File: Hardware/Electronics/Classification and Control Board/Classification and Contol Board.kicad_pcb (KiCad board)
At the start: 4 copper layers, 53.9 x 62.3 mm, 93 parts, among them J1 SWD Header, J10 USB_B_Mini, J2 Barrel_Jack, J3 Thumb, J4 Index, J5 Middle, J6 Ring, J7 Pinky, J8 Wrist, J9 HC05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

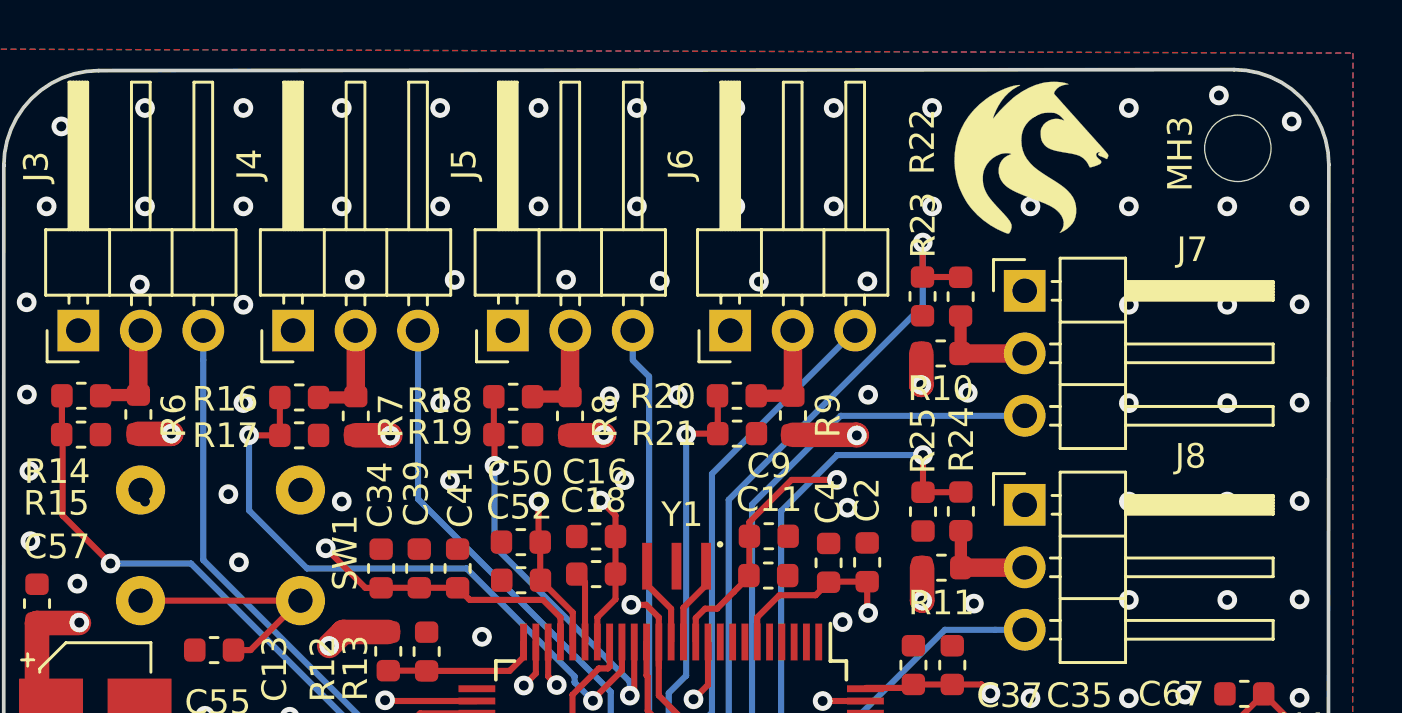
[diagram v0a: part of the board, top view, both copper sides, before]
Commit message: Ran the Gerbers, made fab layer look fab
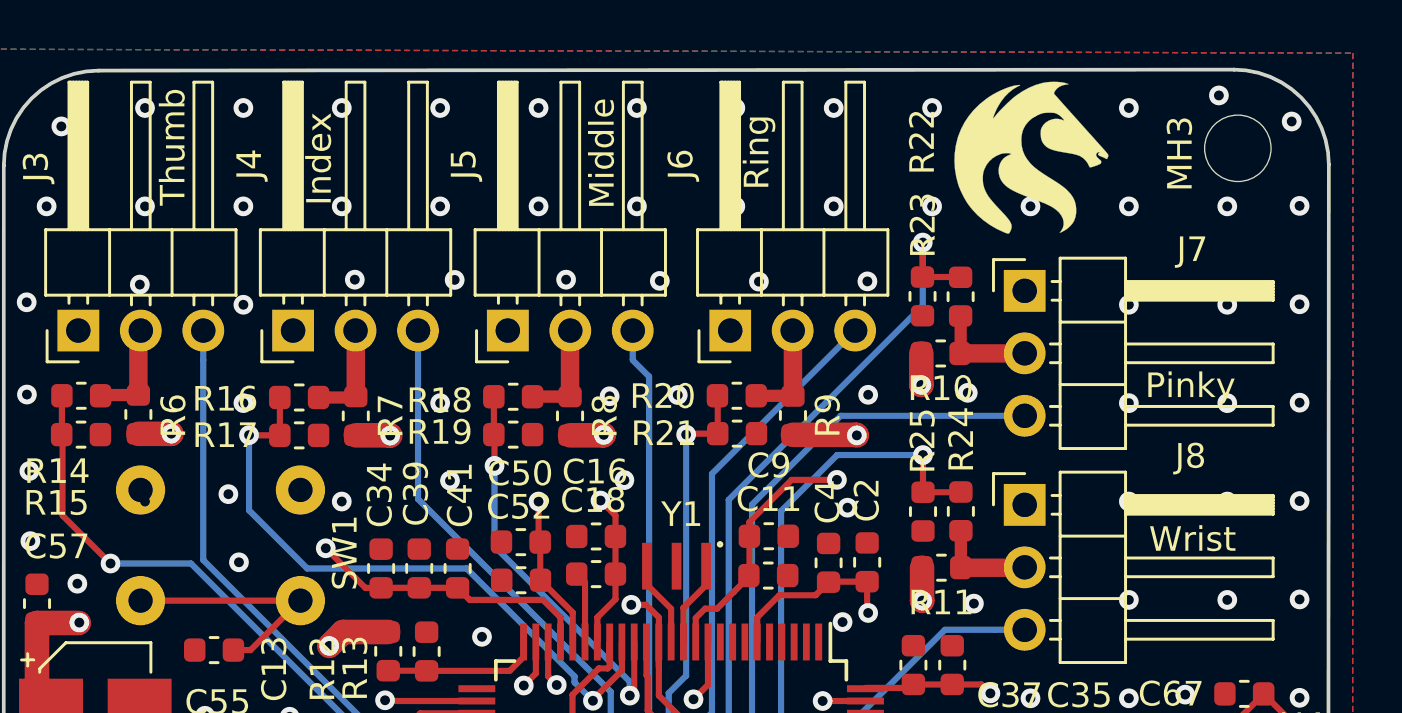
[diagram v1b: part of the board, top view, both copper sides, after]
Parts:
- MH1: value MountingHole -> (none)

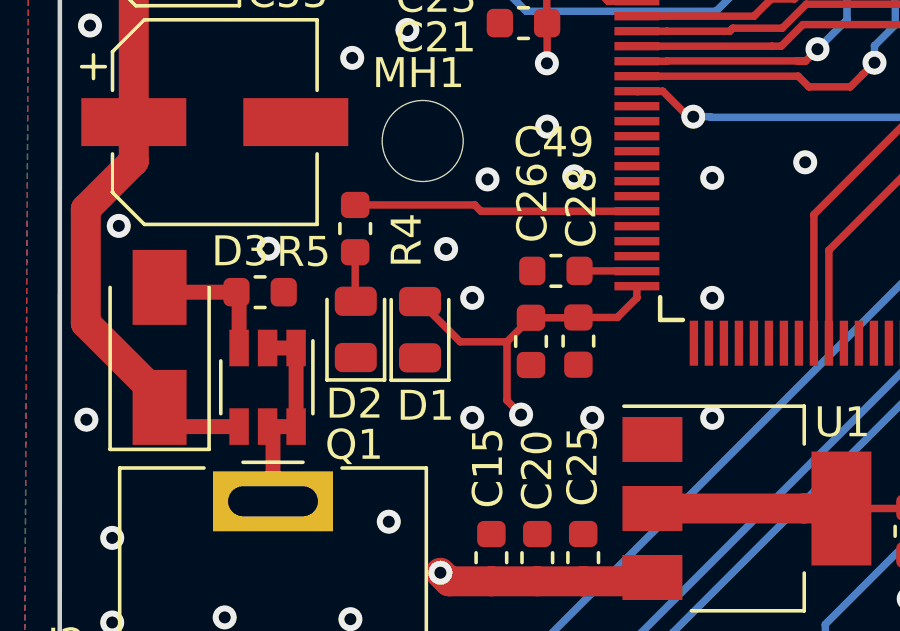
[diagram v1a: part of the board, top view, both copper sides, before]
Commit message: Changed blue LED to green and added current limiting resistor
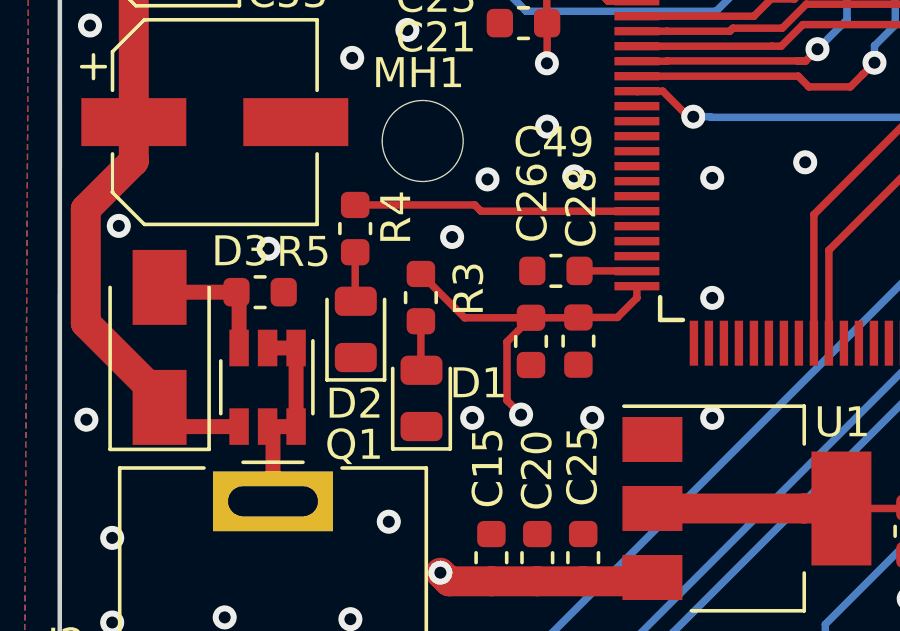
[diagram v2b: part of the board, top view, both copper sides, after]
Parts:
- added R3: 6R, Resistor_SMD:R_0603_1608Metric, F.Cu at (126.5, 98.8)
- D1: value LTST-C171TBKT -> LTST-C171TGKT
- MH1: value (none) -> MountingHole
- moved D1 2.29 mm to (126.5, 102.2)
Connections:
- D1 pad 2: /STM32F407VGTx/3V3 -> Net-(D1-Pad2)
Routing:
- net Net-(D1-Pad2): track 0.00 -> 1.64 mm
- net /STM32F407VGTx/3V3: track 89.5 -> 90.3 mm
- net /GND: vias 176 -> 175
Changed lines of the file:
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@@
     (thickness 1.6)
     (drawings 15)
-    (tracks 722)
+    (tracks 723)
     (zones 0)
-    (modules 93)
-    (nets 122)
+    (modules 94)
+    (nets 123)
   )
   (page A4)
@@
     (34 B.Paste user)
     (35 F.Paste user)
-    (36 B.SilkS user hide)
+    (36 B.SilkS user)
     (37 F.SilkS user)
     (38 B.Mask user)
@@
   (net 120 /Communications/BT_TX)
   (net 121 /Communications/BT_RX)
+  (net 122 "Net-(D1-Pad2)")
   (net_class Default "This is the default net class."
     (clearance 0.15)
@@
     (add_net "Net-(C51-Pad1)")
     (add_net "Net-(C61-Pad1)")
+    (add_net "Net-(D1-Pad2)")
     (add_net "Net-(D2-Pad2)")
     (add_net "Net-(D6-Pad2)")
@@
     (add_net /V+)
   )
+  (module Resistor_SMD:R_0603_1608Metric (layer F.Cu)
+    (at 126.47 98.82 90)
+    (descr "Resistor SMD 0603 (1608 Metric), square (rectangular) end terminal, IPC_7351 nominal, (Body size source: http://www.tortai-tech.com/upload/download/2011102023233369053.pdf), generated with kicad-footprint-generator")
+    (tags resistor)
+    (attr smd)
+    (fp_text reference R3 (at 0.3 1.6 90) (layer F.SilkS)
+      (effects (font (size 1 1) (thickness 0.15)))
+    )
+    (fp_text value 6R (at 0 1.43 90) (layer F.Fab)
+      (effects (font (size 1 1) (thickness 0.15)))
+    )
+    (fp_line (start -0.8 0.4) (end -0.8 -0.4) (layer F.Fab) (width 0.1))
+    (fp_line (start -0.8 -0.4) (end 0.8 -0.4) (layer F.Fab) (width 0.1))
+    (fp_line (start 0.8 -0.4) (end 0.8 0.4) (layer F.Fab) (width 0.1))
+    (fp_line (start 0.8 0.4) (end -0.8 0.4) (layer F.Fab) (width 0.1))
+    (fp_line (start -0.162779 -0.51) (end 0.162779 -0.51) (layer F.SilkS) (width 0.12))
+    (fp_line (start -0.162779 0.51) (end 0.162779 0.51) (layer F.SilkS) (width 0.12))
+    (fp_line (start -1.48 0.73) (end -1.48 -0.73) (layer F.CrtYd) (width 0.05))
+    (fp_line (start -1.48 -0.73) (end 1.48 -0.73) (layer F.CrtYd) (width 0.05))
+    (fp_line (start 1.48 -0.73) (end 1.48 0.73) (layer F.CrtYd) (width 0.05))
+    (fp_line (start 1.48 0.73) (end -1.48 0.73) (layer F.CrtYd) (width 0.05))
+    (fp_text user %R (at 0 0 90) (layer F.Fab)
+      (effects (font (size 0.4 0.4) (thickness 0.06)))
+    )
+    (pad 1 smd roundrect (at -0.7875 0 90) (size 0.875 0.95) (layers F.Cu F.Paste F.Mask) (roundrect_rratio 0.25)
+      (net 122 "Net-(D1-Pad2)"))
+    (pad 2 smd roundrect (at 0.7875 0 90) (size 0.875 0.95) (layers F.Cu F.Paste F.Mask) (roundrect_rratio 0.25)
+      (net 4 /STM32F407VGTx/3V3))
+    (model ${KISYS3DMOD}/Resistor_SMD.3dshapes/R_0603_1608Metric.wrl
+      (at (xyz 0 0 0))
+      (scale (xyz 1 1 1))
+      (rotate (xyz 0 0 0))
+    )
+  )
   (module Switches:1825910-6 (layer F.Cu)
     (at 120 78.36)
@@
   )
   (module LED_SMD:LED_0805_2012Metric (layer F.Cu)
-    (at 126.44 99.89 90)
+    (at 126.49 102.18 90)
     (descr "LED SMD 0805 (2012 Metric), square (rectangular) end terminal, IPC_7351 nominal, (Body size source: https://docs.google.com/spreadsheets/d/1BsfQQcO9C6DZCsRaXUlFlo91Tg2WpOkGARC1WS5S8t0/edit?usp=sharing), generated with kicad-footprint-generator")
     (tags diode)
     (attr smd)
-    (fp_text reference D1 (at -2.54 0.19 180) (layer F.SilkS)
+    (fp_text reference D1 (at 0.5 1.9 180) (layer F.SilkS)
       (effects (font (size 1 1) (thickness 0.15)))
     )
-    (fp_text value LTST-C171TBKT (at -32.12 -0.98 90) (layer F.Fab)
+    (fp_text value LTST-C171TGKT (at -32.12 -0.98 90) (layer F.Fab)
       (effects (font (size 1 1) (thickness 0.15)))
     )
@@
       (net 1 /GND))
     (pad 2 smd roundrect (at 0.9375 0 90) (size 0.975 1.4) (layers F.Cu F.Paste F.Mask) (roundrect_rratio 0.25)
-      (net 4 /STM32F407VGTx/3V3))
+      (net 122 "Net-(D1-Pad2)"))
     (model ${KISYS3DMOD}/LED_SMD.3dshapes/LED_0805_2012Metric.wrl
       (at (xyz 0 0 0))
@@
       (effects (font (size 1 1) (thickness 0.15)))
     )
-    (fp_text value " " (at -21.29 -1.82) (layer F.Fab)
+    (fp_text value MountingHole (at -21.29 -1.82) (layer F.Fab)
       (effects (font (size 1 1) (thickness 0.15)))
     )
@@
     (tags resistor)
     (attr smd)
-    (fp_text reference R4 (at 0.39 -1.72 270) (layer F.SilkS)
+    (fp_text reference R4 (at -0.37 -1.37 270) (layer F.SilkS)
       (effects (font (size 1 1) (thickness 0.15)))
     )
@@
   (via (at 130.68 93.12) (size 0.8) (drill 0.4) (layers F.Cu B.Cu) (net 1))
   (via (at 128.69 94.88) (size 0.8) (drill 0.4) (layers F.Cu B.Cu) (net 1))
-  (via (at 128.18 98.83) (size 0.8) (drill 0.4) (layers F.Cu B.Cu) (net 1))
   (via (at 128.18 102.83) (size 0.8) (drill 0.4) (layers F.Cu B.Cu) (net 1))
   (via (at 128.18 110.83) (size 0.8) (drill 0.4) (layers F.Cu B.Cu) (net 1))
@@
   (via (at 124 81.3) (size 0.8) (drill 0.4) (layers F.Cu B.Cu) (net 1))
   (via (at 124.18 90.83) (size 0.8) (drill 0.4) (layers F.Cu B.Cu) (net 1))
-  (via (at 127.31 97.2) (size 0.8) (drill 0.4) (layers F.Cu B.Cu) (net 1))
+  (via (at 127.51 96.8) (size 0.8) (drill 0.4) (layers F.Cu B.Cu) (net 1))
   (via (at 125.4 106.29) (size 0.8) (drill 0.4) (layers F.Cu B.Cu) (net 1))
   (via (at 124.12 109.54) (size 0.8) (drill 0.4) (layers F.Cu B.Cu) (net 1))
@@
   (segment (start 136.18 80.4125) (end 136.2475 80.48) (width 0.25) (layer F.Cu) (net 4))
   (segment (start 136.18 78.83) (end 136.18 80.4125) (width 0.25) (layer F.Cu) (net 4))
-  (segment (start 127.78001 100.29251) (end 126.44 98.9525) (width 0.25) (layer F.Cu) (net 4))
-  (segment (start 129.33999 100.29251) (end 127.78001 100.29251) (width 0.25) (layer F.Cu) (net 4))
   (segment (start 131.3675 87.44) (end 130.6675 88.14) (width 0.25) (layer F.Cu) (net 4))
   (segment (start 133.67 87.44) (end 131.3675 87.44) (width 0.25) (layer F.Cu) (net 4))
@@
   (segment (start 149.90001 104.64999) (end 149.90001 103.33251) (width 0.25) (layer F.Cu) (net 4))
   (segment (start 149.14 105.41) (end 149.90001 104.64999) (width 0.25) (layer F.Cu) (net 4))
+  (segment (start 127.93 99.4925) (end 126.47 98.0325) (width 0.25) (layer F.Cu) (net 4))
+  (segment (start 130.14 99.4925) (end 127.93 99.4925) (width 0.25) (layer F.Cu) (net 4))
   (segment (start 152.32 88.5325) (end 152.5225 88.33) (width 0.25) (layer F.Cu) (net 5))
   (segment (start 150.47 89.44) (end 149.47 89.44) (width 0.25) (layer F.Cu) (net 5))
@@
   (segment (start 150.995001 107.505001) (end 151.504005 107.505001) (width 0.25) (layer B.Cu) (net 121))
   (segment (start 150.59 107.1) (end 150.995001 107.505001) (width 0.25) (layer B.Cu) (net 121))
+  (segment (start 126.47 101.2225) (end 126.49 101.2425) (width 0.25) (layer F.Cu) (net 122))
+  (segment (start 126.47 99.6075) (end 126.47 101.2225) (width 0.25) (layer F.Cu) (net 122))
   (zone (net 1) (net_name /GND) (layer F.Cu) (hatch edge 0.508)
     (connect_pads (clearance 0.3))

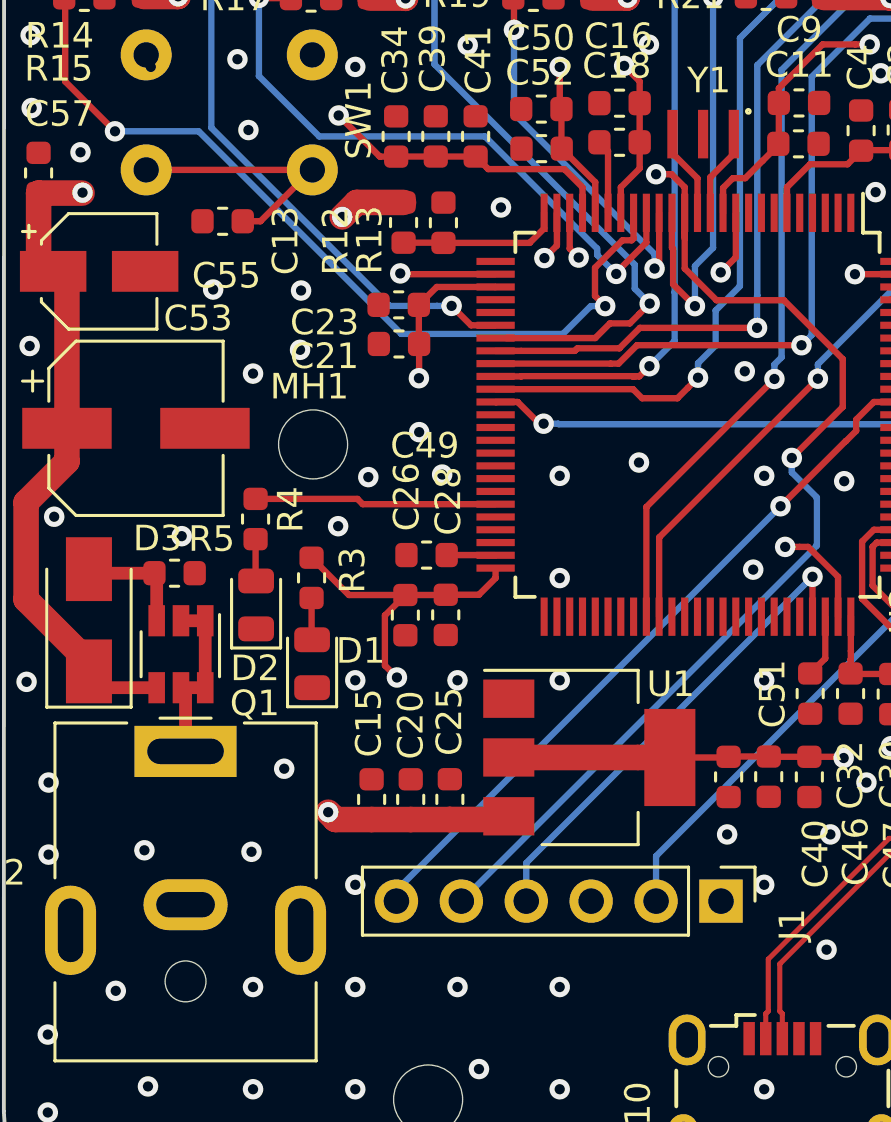
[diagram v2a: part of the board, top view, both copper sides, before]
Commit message: Changed hardware to make USB use USART2 to be binary compatible with Dev Board. Moved some components accordingly.
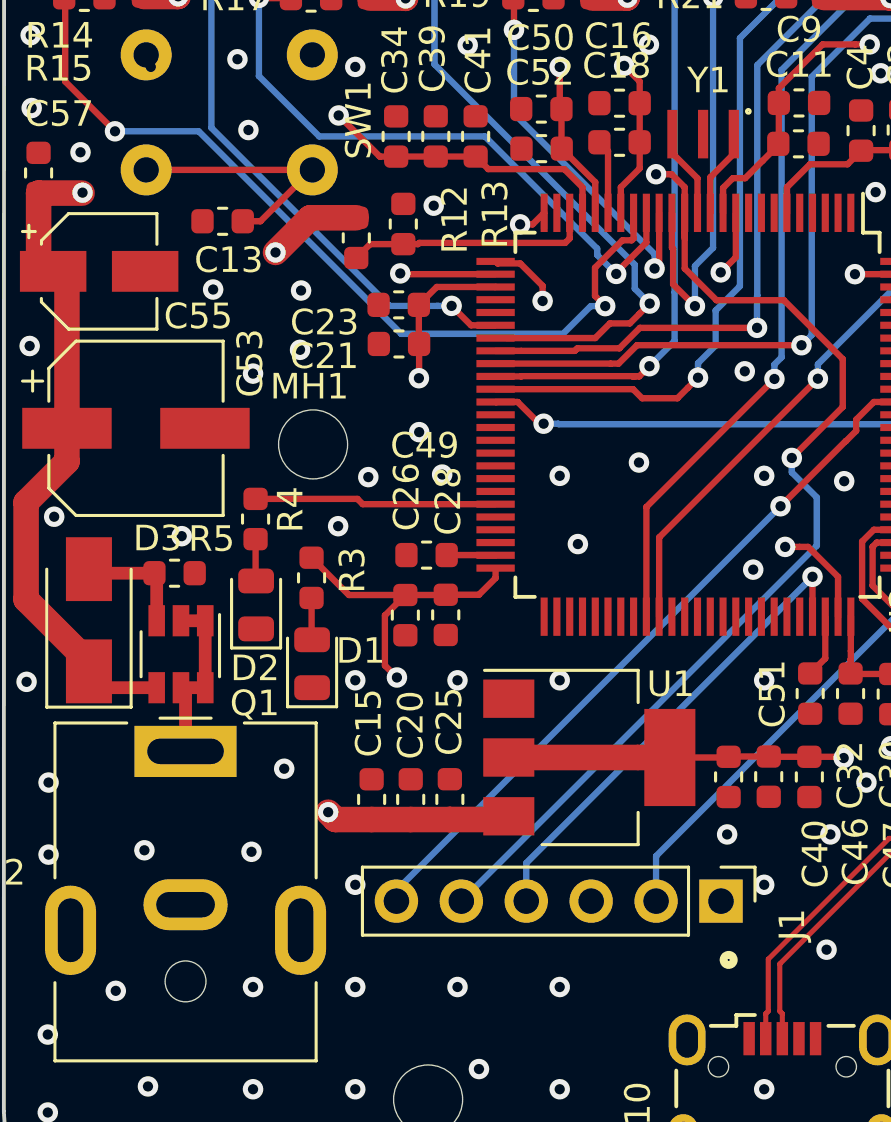
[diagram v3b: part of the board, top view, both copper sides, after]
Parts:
- R4: value 65R -> 68R
- Y1: value 12MHz -> 8MHz
- moved R12 1.94 mm to (128.2, 85.5)
- moved R13 1.57 mm to (130.1, 85.0)
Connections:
- U2 pad 23: /Communications/TX -> /Control/FB_REF
- U2 pad 24: /Communications/RX -> Net-(U2-Pad24)
- U2 pad 25: /Control/FB_REF -> /Communications/TX
- U2 pad 26: Net-(U2-Pad26) -> /Communications/RX
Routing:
- net /Control/FB_REF: track 6.35 -> 9.67 mm
- net /Communications/TX: track 33.0 -> 35.1 mm
- net /V+: track 50.1 -> 51.2 mm
- net /Communications/RX: track 35.3 -> 34.5 mm

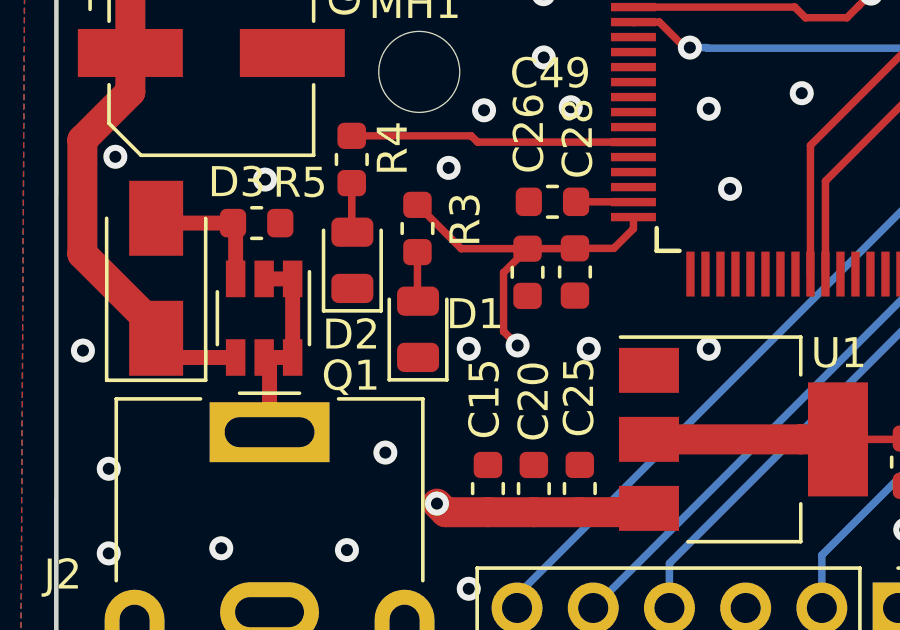
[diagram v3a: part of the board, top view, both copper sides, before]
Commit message: BoM Updates, fixed D1 footprint from 0805 to 0603
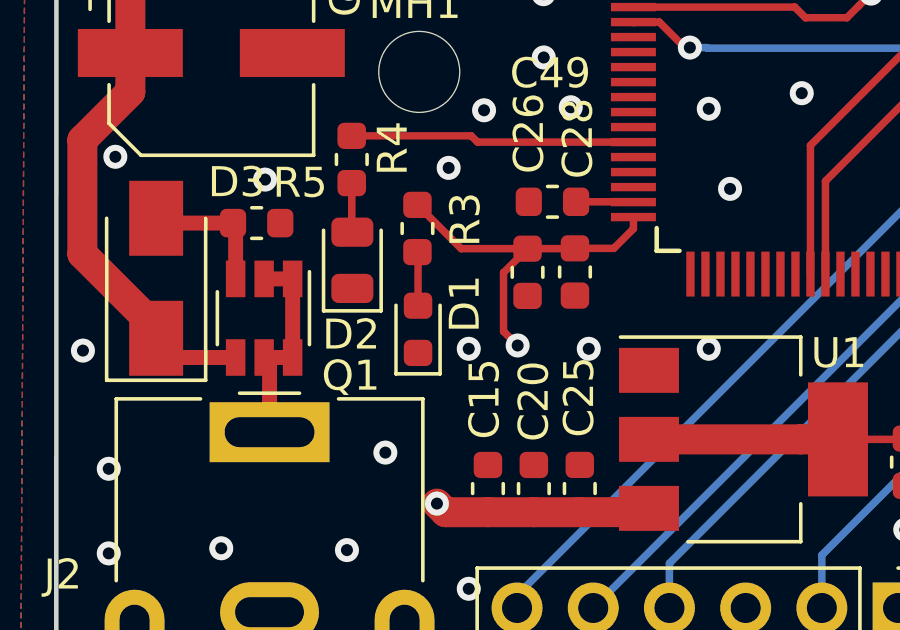
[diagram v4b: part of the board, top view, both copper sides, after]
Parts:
- D1: footprint LED_SMD:LED_0805_2012Metric -> LED_SMD:LED_0603_1608Metric
